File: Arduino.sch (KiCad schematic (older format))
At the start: 0 parts

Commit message: Overall Schematic
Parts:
- added R? (x13): R, ~, symbol R
- added U?: ARDUINOPINS, symbol ARDUINOPINS
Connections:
- net MISO: now also R?.2
- net MOSI: now also R?.2
- net SCLK: now also R?.2
- net TACH_MEAS: now also R?.1
- new net: R?.1, U?.11 (Digital0)
- new net: R?.1, U?.12 (Digital1)
- new net: R?.1, U?.19 (Digital8)
- new net: R?.1, U?.20 (PWM0)
- new net: R?.1, U?.21 (CS_N)
- new net: R?.1, U?.22 (MOSI)
- new net: R?.1, U?.23 (MISO)
- new net: R?.1, U?.24 (SCK)
- new net: R?.2, U?.5 (AnalogIn0)
- new net: R?.2, U?.6 (AnalogIn1)
- new net: R?.2, U?.7 (AnalogIn2)
- new net: R?.2, U?.8 (AnalogIn3)
- new net ADC_CS_N: R?.2
- new net CURR_MEAS: R?.1
- new net DAC_CS_N: R?.2
- new net FAN_EN_N: R?.2
- new net GND: R?.1
- new net LED_EN_PWM: R?.2
- new net RELAY+: R?.2
- new net RELAY-: R?.2
- new net V+_ADJ_MON: R?.1
- new net V-_ADJ_MON: R?.1
- no-connect marks 0 -> 1

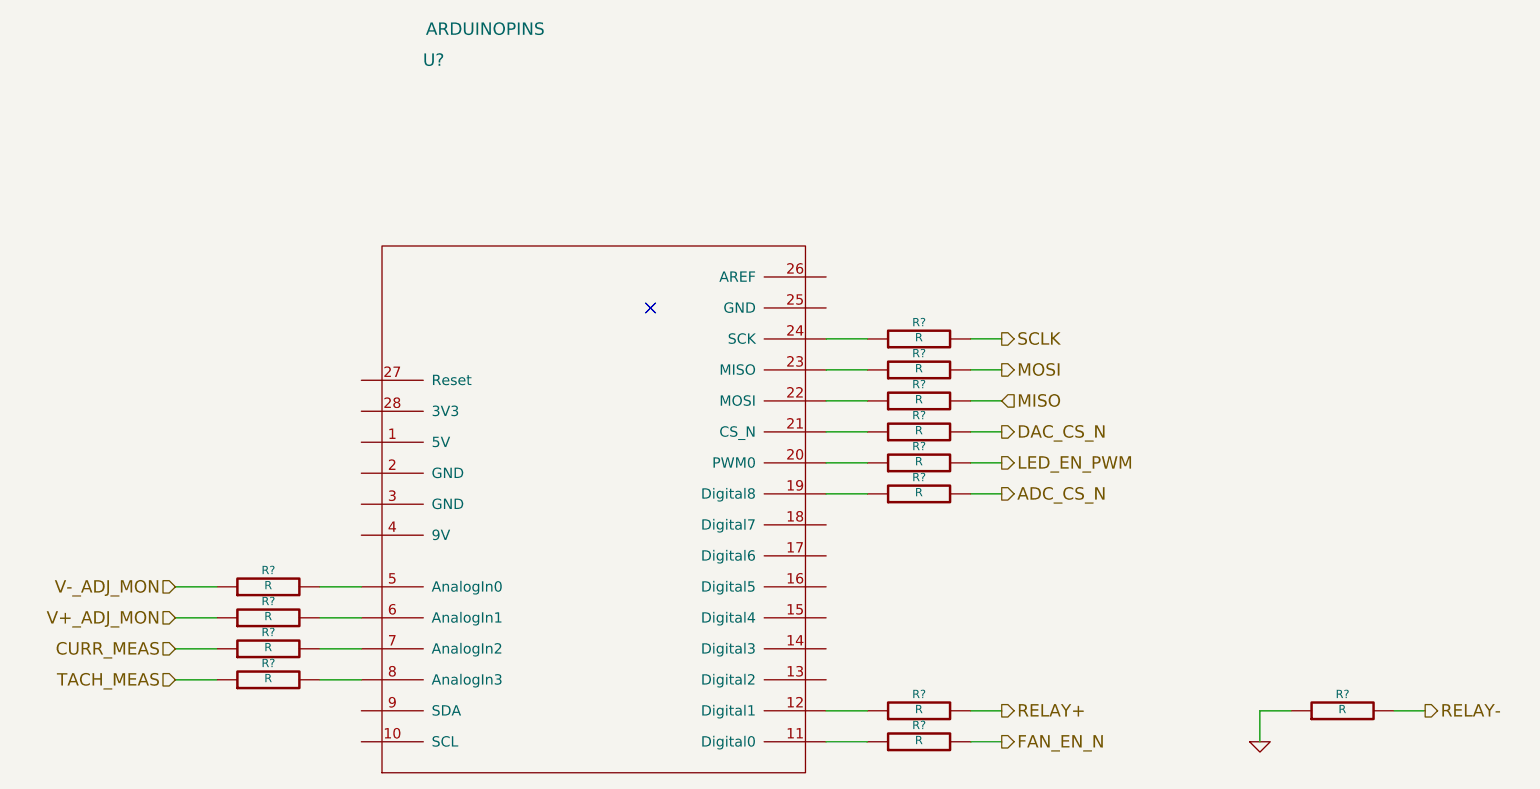
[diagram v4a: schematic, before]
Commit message: Fan/Current Module Refactoring
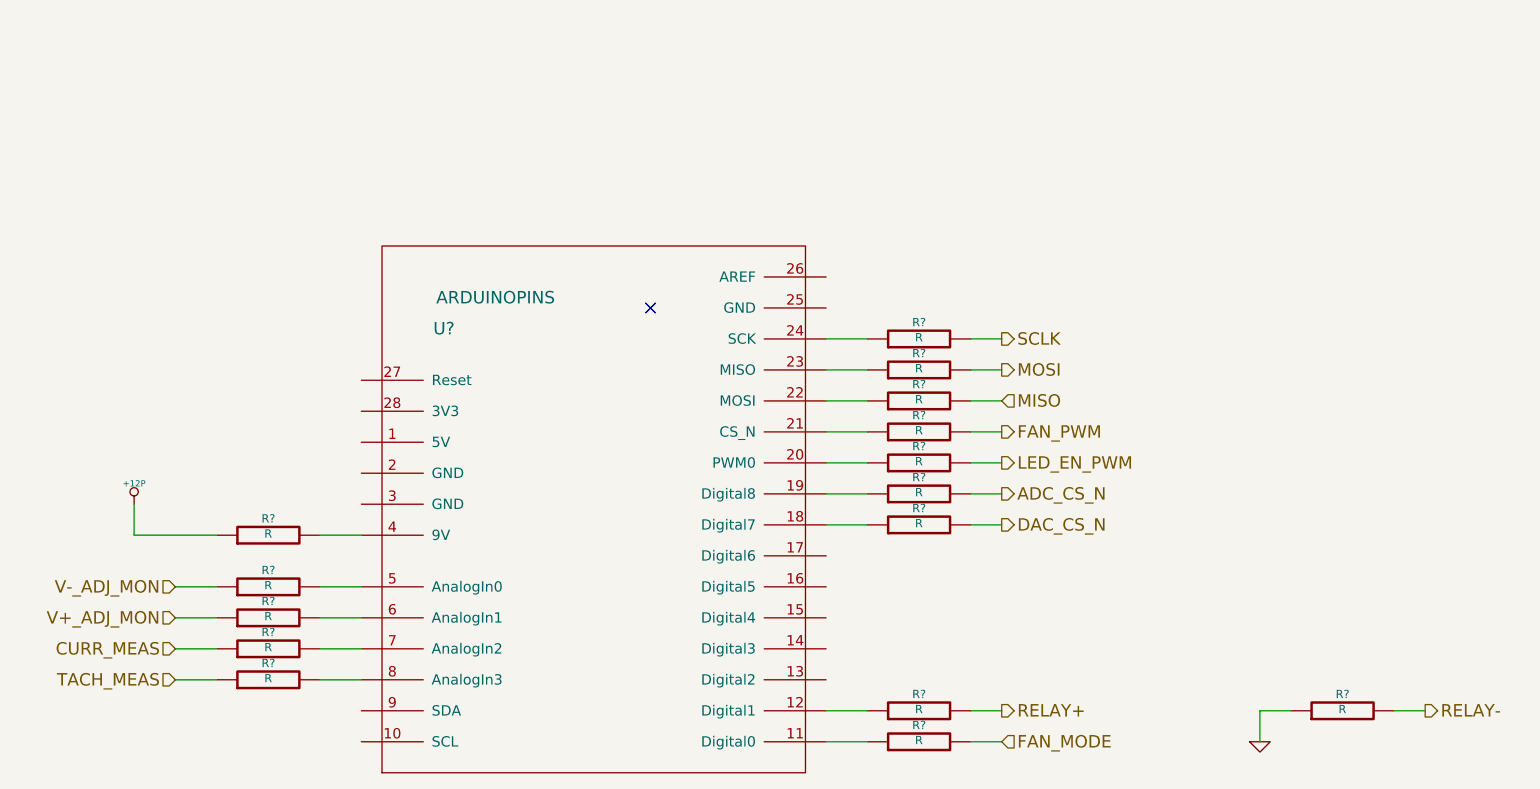
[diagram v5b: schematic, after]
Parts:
- added R? (x2): R, ~, symbol R
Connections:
- net at U?.11 (Digital0): now also R?.1; no longer R?.1
- net at U?.18 (Digital7): now also R?.1
- net at U?.21 (CS_N): now also R?.1; no longer R?.1
- net at U?.4 (9V): now also R?.2
- net FAN_EN_N renamed FAN_PWM
- new net +12P: R?.1
- new net FAN_MODE: R?.2
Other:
- moved on the sheet: R?
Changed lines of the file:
@@
 $Descr A4 11693 8268
 encoding utf-8
-Sheet 2 9
+Sheet 8 9
 Title ""
-Date "28 sep 2013"
+Date "30 sep 2013"
 Rev ""
 Comp ""
@@
 Comment4 ""
 $EndDescr
-Text HLabel 7300 5900 2    60   Output ~ 0
-FAN_EN_N
+Text HLabel 7300 4400 2    60   Output ~ 0
+FAN_PWM
 Text HLabel 3300 5600 0    60   Input ~ 0
 TACH_MEAS
@@
 Text HLabel 7300 3950 2    60   Output ~ 0
 SCLK
-Text HLabel 7300 4400 2    60   Output ~ 0
+Text HLabel 7300 4850 2    60   Output ~ 0
 DAC_CS_N
 Text HLabel 7300 5750 2    60   Output ~ 0
@@
 U 1 1 524756E9
 P 5350 4800
-F 0 "U?" H 4550 7000 60  0000 C CNN
-F 1 "ARDUINOPINS" H 4800 7150 60  0000 C CNN
+F 0 "U?" H 4600 5700 60  0000 C CNN
+F 1 "ARDUINOPINS" H 4850 5850 60  0000 C CNN
 F 2 "" H 5350 4800 60  0000 C CNN
 F 3 "" H 5350 4800 60  0000 C CNN
@@
 L R R?
 U 1 1 5247573B
-P 6900 5900
-F 0 "R?" V 6980 5900 40  0000 C CNN
-F 1 "R" V 6907 5901 40  0000 C CNN
-F 2 "~" V 6830 5900 30  0000 C CNN
-F 3 "~" H 6900 5900 30  0000 C CNN
-	1    6900 5900
-	0    -1   -1   0
-$EndComp
-Wire Wire Line
-	7150 5900 7300 5900
-Wire Wire Line
-	6650 5900 6450 5900
+P 6900 4400
+F 0 "R?" V 6980 4400 40  0000 C CNN
+F 1 "R" V 6907 4401 40  0000 C CNN
+F 2 "~" V 6830 4400 30  0000 C CNN
+F 3 "~" H 6900 4400 30  0000 C CNN
+	1    6900 4400
+	0    -1   -1   0
+$EndComp
+Wire Wire Line
+	7150 4400 7300 4400
+Wire Wire Line
+	6650 4400 6450 4400
 $Comp
 L R R?
@@
 L R R?
 U 1 1 5247E718
-P 6900 4400
-F 0 "R?" V 6980 4400 40  0000 C CNN
-F 1 "R" V 6907 4401 40  0000 C CNN
-F 2 "~" V 6830 4400 30  0000 C CNN
-F 3 "~" H 6900 4400 30  0000 C CNN
-	1    6900 4400
+P 6900 4850
+F 0 "R?" V 6980 4850 40  0000 C CNN
+F 1 "R" V 6907 4851 40  0000 C CNN
+F 2 "~" V 6830 4850 30  0000 C CNN
+F 3 "~" H 6900 4850 30  0000 C CNN
+	1    6900 4850
 	0    -1   -1   0
 $EndComp
@@
 	7150 4250 7300 4250
 Wire Wire Line
-	7150 4400 7300 4400
-Wire Wire Line
 	6450 3950 6650 3950
 Wire Wire Line
@@
 Wire Wire Line
 	6450 4250 6650 4250
-Wire Wire Line
-	6450 4400 6650 4400
 $Comp
 L R R?
@@
 Wire Wire Line
 	6650 4700 6450 4700
+Wire Wire Line
+	7150 4850 7300 4850
+Wire Wire Line
+	6450 4850 6650 4850
+Text HLabel 7300 5900 2    60   Input ~ 0
+FAN_MODE
+$Comp
+L R R?
+U 1 1 524B6E8B
+P 6900 5900
+F 0 "R?" V 6980 5900 40  0000 C CNN
+F 1 "R" V 6907 5901 40  0000 C CNN
+F 2 "~" V 6830 5900 30  0000 C CNN
+F 3 "~" H 6900 5900 30  0000 C CNN
+	1    6900 5900
+	0    -1   -1   0
+$EndComp
+Wire Wire Line
+	6450 5900 6650 5900
+Wire Wire Line
+	7150 5900 7300 5900
+$Comp
+L R R?
+U 1 1 524B7119
+P 3750 4900
+F 0 "R?" V 3830 4900 40  0000 C CNN
+F 1 "R" V 3757 4901 40  0000 C CNN
+F 2 "~" V 3680 4900 30  0000 C CNN
+F 3 "~" H 3750 4900 30  0000 C CNN
+	1    3750 4900
+	0    -1   -1   0
+$EndComp
+Wire Wire Line
+	3500 4900 3100 4900
+Wire Wire Line
+	3100 4900 3100 4750
+Wire Wire Line
+	4000 4900 4200 4900
+$Comp
+L +12P #PWR?
+U 1 1 524B7161
+P 3100 4750
+F 0 "#PWR?" H 3100 4720 30  0001 C CNN
+F 1 "+12P" H 3100 4850 30  0000 C CNN
+F 2 "" H 3100 4750 60  0000 C CNN
+F 3 "" H 3100 4750 60  0000 C CNN
+	1    3100 4750
+	1    0    0    -1
+$EndComp
 $EndSCHEMATC

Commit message: Preliminary Module Layouts
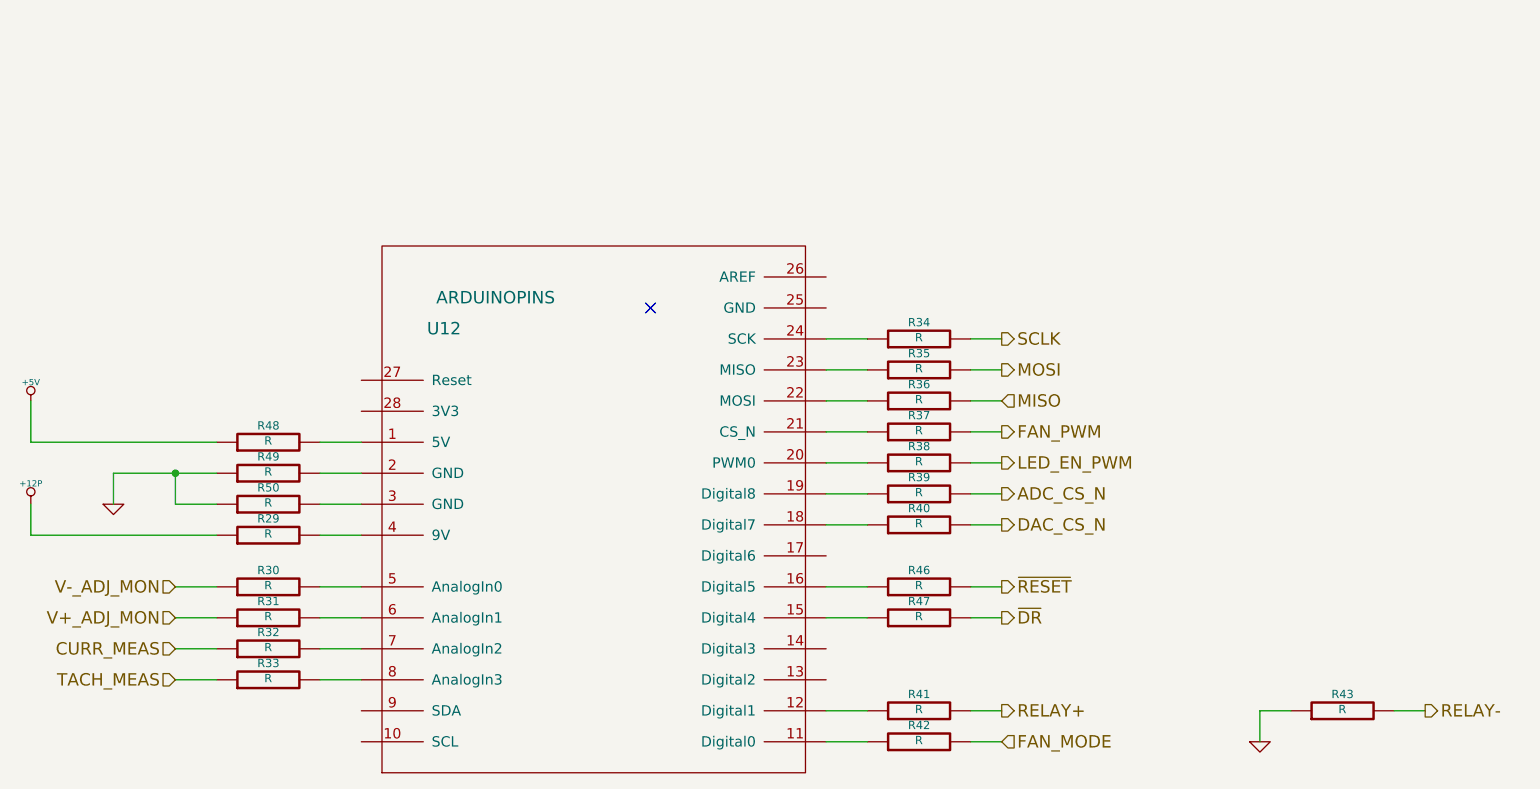
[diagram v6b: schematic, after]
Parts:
- added R46, R47, R48, R49, R50: R, ~, symbol R
- gave numbers to parts that had none: 16
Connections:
- net GND: now also R49.1, R50.1
- net at U12.1 (5V): now also R48.2
- net at U12.15 (Digital4): now also R47.1
- net at U12.16 (Digital5): now also R46.1
- net at U12.2 (GND): now also R49.2
- net at U12.3 (GND): now also R50.2
- new net +5V: R48.1
- new net ~DR: R47.2
- new net ~RESET: R46.2
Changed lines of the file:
@@
 Sheet 8 9
 Title ""
-Date "30 sep 2013"
+Date "15 oct 2013"
 Rev ""
 Comp ""
@@
 NoConn ~ 5600 3800
 $Comp
-L ARDUINOPINS U?
+L ARDUINOPINS U12
 U 1 1 524756E9
 P 5350 4800
-F 0 "U?" H 4600 5700 60  0000 C CNN
+F 0 "U12" H 4600 5700 60  0000 C CNN
 F 1 "ARDUINOPINS" H 4850 5850 60  0000 C CNN
 F 2 "" H 5350 4800 60  0000 C CNN
@@
 CURR_MEAS
 $Comp
-L R R?
+L R R37
 U 1 1 5247573B
 P 6900 4400
-F 0 "R?" V 6980 4400 40  0000 C CNN
+F 0 "R37" V 6980 4400 40  0000 C CNN
 F 1 "R" V 6907 4401 40  0000 C CNN
 F 2 "~" V 6830 4400 30  0000 C CNN
@@
 	6650 4400 6450 4400
 $Comp
-L R R?
+L R R41
 U 1 1 5247DC4C
 P 6900 5750
-F 0 "R?" V 6980 5750 40  0000 C CNN
+F 0 "R41" V 6980 5750 40  0000 C CNN
 F 1 "R" V 6907 5751 40  0000 C CNN
 F 2 "~" V 6830 5750 30  0000 C CNN
@@
 	8550 5750 8550 5900
 $Comp
-L GND #PWR?
+L GND #PWR053
 U 1 1 5247DC74
 P 8550 5900
-F 0 "#PWR?" H 8550 5900 30  0001 C CNN
+F 0 "#PWR053" H 8550 5900 30  0001 C CNN
 F 1 "GND" H 8550 5830 30  0001 C CNN
 F 2 "" H 8550 5900 60  0000 C CNN
@@
 $EndComp
 $Comp
-L R R?
+L R R32
 U 1 1 5247DC8B
 P 3750 5450
-F 0 "R?" V 3830 5450 40  0000 C CNN
+F 0 "R32" V 3830 5450 40  0000 C CNN
 F 1 "R" V 3757 5451 40  0000 C CNN
 F 2 "~" V 3680 5450 30  0000 C CNN
@@
 $EndComp
 $Comp
-L R R?
+L R R33
 U 1 1 5247DC91
 P 3750 5600
-F 0 "R?" V 3830 5600 40  0000 C CNN
+F 0 "R33" V 3830 5600 40  0000 C CNN
 F 1 "R" V 3757 5601 40  0000 C CNN
 F 2 "~" V 3680 5600 30  0000 C CNN
@@
 V-_ADJ_MON
 $Comp
-L R R?
+L R R30
 U 1 1 5247E210
 P 3750 5150
-F 0 "R?" V 3830 5150 40  0000 C CNN
+F 0 "R30" V 3830 5150 40  0000 C CNN
 F 1 "R" V 3757 5151 40  0000 C CNN
 F 2 "~" V 3680 5150 30  0000 C CNN
@@
 $EndComp
 $Comp
-L R R?
+L R R31
 U 1 1 5247E216
 P 3750 5300
-F 0 "R?" V 3830 5300 40  0000 C CNN
+F 0 "R31" V 3830 5300 40  0000 C CNN
 F 1 "R" V 3757 5301 40  0000 C CNN
 F 2 "~" V 3680 5300 30  0000 C CNN
@@
 	4000 5300 4200 5300
 $Comp
-L R R?
+L R R34
 U 1 1 5247E706
 P 6900 3950
-F 0 "R?" V 6980 3950 40  0000 C CNN
+F 0 "R34" V 6980 3950 40  0000 C CNN
 F 1 "R" V 6907 3951 40  0000 C CNN
 F 2 "~" V 6830 3950 30  0000 C CNN
@@
 $EndComp
 $Comp
-L R R?
+L R R35
 U 1 1 5247E70C
 P 6900 4100
-F 0 "R?" V 6980 4100 40  0000 C CNN
+F 0 "R35" V 6980 4100 40  0000 C CNN
 F 1 "R" V 6907 4101 40  0000 C CNN
 F 2 "~" V 6830 4100 30  0000 C CNN
@@
 $EndComp
 $Comp
-L R R?
+L R R36
 U 1 1 5247E712
 P 6900 4250
-F 0 "R?" V 6980 4250 40  0000 C CNN
+F 0 "R36" V 6980 4250 40  0000 C CNN
 F 1 "R" V 6907 4251 40  0000 C CNN
 F 2 "~" V 6830 4250 30  0000 C CNN
@@
 $EndComp
 $Comp
-L R R?
+L R R40
 U 1 1 5247E718
 P 6900 4850
-F 0 "R?" V 6980 4850 40  0000 C CNN
+F 0 "R40" V 6980 4850 40  0000 C CNN
 F 1 "R" V 6907 4851 40  0000 C CNN
 F 2 "~" V 6830 4850 30  0000 C CNN
@@
 	6450 4250 6650 4250
 $Comp
-L R R?
+L R R43
 U 1 1 5247EA04
 P 8950 5750
-F 0 "R?" V 9030 5750 40  0000 C CNN
+F 0 "R43" V 9030 5750 40  0000 C CNN
 F 1 "R" V 8957 5751 40  0000 C CNN
 F 2 "~" V 8880 5750 30  0000 C CNN
@@
 LED_EN_PWM
 $Comp
-L R R?
+L R R38
 U 1 1 5247EC74
 P 6900 4550
-F 0 "R?" V 6980 4550 40  0000 C CNN
+F 0 "R38" V 6980 4550 40  0000 C CNN
 F 1 "R" V 6907 4551 40  0000 C CNN
 F 2 "~" V 6830 4550 30  0000 C CNN
@@
 	6450 4550 6650 4550
 $Comp
-L R R?
+L R R39
 U 1 1 5249FE11
 P 6900 4700
-F 0 "R?" V 6980 4700 40  0000 C CNN
+F 0 "R39" V 6980 4700 40  0000 C CNN
 F 1 "R" V 6907 4701 40  0000 C CNN
 F 2 "~" V 6830 4700 30  0000 C CNN
@@
 FAN_MODE
 $Comp
-L R R?
+L R R42
 U 1 1 524B6E8B
 P 6900 5900
-F 0 "R?" V 6980 5900 40  0000 C CNN
+F 0 "R42" V 6980 5900 40  0000 C CNN
 F 1 "R" V 6907 5901 40  0000 C CNN
 F 2 "~" V 6830 5900 30  0000 C CNN
@@
 	7150 5900 7300 5900
 $Comp
-L R R?
+L R R29
 U 1 1 524B7119
 P 3750 4900
-F 0 "R?" V 3830 4900 40  0000 C CNN
+F 0 "R29" V 3830 4900 40  0000 C CNN
 F 1 "R" V 3757 4901 40  0000 C CNN
 F 2 "~" V 3680 4900 30  0000 C CNN
@@
 $EndComp
 Wire Wire Line
-	3500 4900 3100 4900
-Wire Wire Line
-	3100 4900 3100 4750
+	3500 4900 2600 4900
+Wire Wire Line
+	2600 4900 2600 4750
 Wire Wire Line
 	4000 4900 4200 4900
 $Comp
-L +12P #PWR?
+L +12P #PWR054
 U 1 1 524B7161
-P 3100 4750
-F 0 "#PWR?" H 3100 4720 30  0001 C CNN
-F 1 "+12P" H 3100 4850 30  0000 C CNN
-F 2 "" H 3100 4750 60  0000 C CNN
-F 3 "" H 3100 4750 60  0000 C CNN
-	1    3100 4750
+P 2600 4750
+F 0 "#PWR054" H 2600 4720 30  0001 C CNN
+F 1 "+12P" H 2600 4850 30  0000 C CNN
+F 2 "" H 2600 4750 60  0000 C CNN
+F 3 "" H 2600 4750 60  0000 C CNN
+	1    2600 4750
 	1    0    0    -1
 $EndComp
+$Comp
+L R R46
+U 1 1 525BB685
+P 6900 5150
+F 0 "R46" V 6980 5150 40  0000 C CNN
+F 1 "R" V 6907 5151 40  0000 C CNN
+F 2 "~" V 6830 5150 30  0000 C CNN
+F 3 "~" H 6900 5150 30  0000 C CNN
+	1    6900 5150
+	0    -1   -1   0
+$EndComp
+$Comp
+L R R47
+U 1 1 525BB68B
+P 6900 5300
+F 0 "R47" V 6980 5300 40  0000 C CNN
+F 1 "R" V 6907 5301 40  0000 C CNN
+F 2 "~" V 6830 5300 30  0000 C CNN
+F 3 "~" H 6900 5300 30  0000 C CNN
+	1    6900 5300
+	0    -1   -1   0
+$EndComp
+Wire Wire Line
+	6450 5150 6650 5150
+Wire Wire Line
+	6650 5300 6450 5300
+Wire Wire Line
+	7150 5150 7300 5150
+Wire Wire Line
+	7150 5300 7300 5300
+Text HLabel 7300 5150 2    60   Output ~ 0
+~RESET
+Text HLabel 7300 5300 2    60   Output ~ 0
+~DR
+$Comp
+L R R50
+U 1 1 525DA883
+P 3750 4750
+F 0 "R50" V 3830 4750 40  0000 C CNN
+F 1 "R" V 3757 4751 40  0000 C CNN
+F 2 "~" V 3680 4750 30  0000 C CNN
+F 3 "~" H 3750 4750 30  0000 C CNN
+	1    3750 4750
+	0    -1   -1   0
+$EndComp
+$Comp
+L R R49
+U 1 1 525DA889
+P 3750 4600
+F 0 "R49" V 3830 4600 40  0000 C CNN
+F 1 "R" V 3757 4601 40  0000 C CNN
+F 2 "~" V 3680 4600 30  0000 C CNN
+F 3 "~" H 3750 4600 30  0000 C CNN
+	1    3750 4600
+	0    -1   -1   0
+$EndComp
+$Comp
+L R R48
+U 1 1 525DA88F
+P 3750 4450
+F 0 "R48" V 3830 4450 40  0000 C CNN
+F 1 "R" V 3757 4451 40  0000 C CNN
+F 2 "~" V 3680 4450 30  0000 C CNN
+F 3 "~" H 3750 4450 30  0000 C CNN
+	1    3750 4450
+	0    -1   -1   0
+$EndComp
+Wire Wire Line
+	2600 4450 3500 4450
+Wire Wire Line
+	2600 4250 2600 4450
+Wire Wire Line
+	3500 4750 3300 4750
+Wire Wire Line
+	3300 4750 3300 4600
+Wire Wire Line
+	3000 4600 3500 4600
+Wire Wire Line
+	3000 4600 3000 4750
+Connection ~ 3300 4600
+$Comp
+L GND #PWR055
+U 1 1 525DA913
+P 3000 4750
+F 0 "#PWR055" H 3000 4750 30  0001 C CNN
+F 1 "GND" H 3000 4680 30  0001 C CNN
+F 2 "" H 3000 4750 60  0000 C CNN
+F 3 "" H 3000 4750 60  0000 C CNN
+	1    3000 4750
+	1    0    0    -1
+$EndComp
+$Comp
+L +5V #PWR056
+U 1 1 525DA94E
+P 2600 4250
+F 0 "#PWR056" H 2600 4340 20  0001 C CNN
+F 1 "+5V" H 2600 4340 30  0000 C CNN
+F 2 "" H 2600 4250 60  0000 C CNN
+F 3 "" H 2600 4250 60  0000 C CNN
+	1    2600 4250
+	1    0    0    -1
+$EndComp
+Wire Wire Line
+	4000 4450 4200 4450
+Wire Wire Line
+	4200 4600 4000 4600
+Wire Wire Line
+	4000 4750 4200 4750
 $EndSCHEMATC

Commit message: Power Modification Module
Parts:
- added R24, R51: R, ~, symbol R
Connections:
- net at U12.13 (Digital2): now also R51.1
- net at U12.14 (Digital3): now also R24.1
- net ADC_CS_N renamed ~ADC_CS
- net DAC_CS_N renamed ~DAC_CS
- new net ~LDAC: R24.2
- new net ~SHDN: R51.2
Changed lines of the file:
@@
 Sheet 8 9
 Title ""
-Date "17 oct 2013"
+Date "27 oct 2013"
 Rev ""
 Comp ""
@@
 SCLK
 Text HLabel 7300 4850 2    60   Output ~ 0
-DAC_CS_N
+~DAC_CS
 Text HLabel 7300 5750 2    60   Output ~ 0
 RELAY+
@@
 	8550 5750 8550 5900
 $Comp
-L GND #PWR053
+L GND #PWR66
 U 1 1 5247DC74
 P 8550 5900
-F 0 "#PWR053" H 8550 5900 30  0001 C CNN
+F 0 "#PWR66" H 8550 5900 30  0001 C CNN
 F 1 "GND" H 8550 5830 30  0001 C CNN
 F 2 "" H 8550 5900 60  0000 C CNN
@@
 $EndComp
 Text HLabel 7300 4700 2    60   Output ~ 0
-ADC_CS_N
+~ADC_CS
 Wire Wire Line
 	7300 4700 7150 4700
@@
 	4000 4900 4200 4900
 $Comp
-L +12P #PWR054
+L +12P #PWR64
 U 1 1 524B7161
 P 2600 4750
-F 0 "#PWR054" H 2600 4720 30  0001 C CNN
+F 0 "#PWR64" H 2600 4720 30  0001 C CNN
 F 1 "+12P" H 2600 4850 30  0000 C CNN
 F 2 "" H 2600 4750 60  0000 C CNN
@@
 Connection ~ 3300 4600
 $Comp
-L GND #PWR055
+L GND #PWR65
 U 1 1 525DA913
 P 3000 4750
-F 0 "#PWR055" H 3000 4750 30  0001 C CNN
+F 0 "#PWR65" H 3000 4750 30  0001 C CNN
 F 1 "GND" H 3000 4680 30  0001 C CNN
 F 2 "" H 3000 4750 60  0000 C CNN
@@
 $EndComp
 $Comp
-L +5V #PWR056
+L +5V #PWR63
 U 1 1 525DA94E
 P 2600 4250
-F 0 "#PWR056" H 2600 4340 20  0001 C CNN
+F 0 "#PWR63" H 2600 4340 20  0001 C CNN
 F 1 "+5V" H 2600 4340 30  0000 C CNN
 F 2 "" H 2600 4250 60  0000 C CNN
@@
 Wire Wire Line
 	4000 4750 4200 4750
+$Comp
+L R R24
+U 1 1 526430CB
+P 6900 5450
+F 0 "R24" V 6980 5450 40  0000 C CNN
+F 1 "R" V 6907 5451 40  0000 C CNN
+F 2 "~" V 6830 5450 30  0000 C CNN
+F 3 "~" H 6900 5450 30  0000 C CNN
+	1    6900 5450
+	0    -1   -1   0
+$EndComp
+$Comp
+L R R51
+U 1 1 526430D1
+P 6900 5600
+F 0 "R51" V 6980 5600 40  0000 C CNN
+F 1 "R" V 6907 5601 40  0000 C CNN
+F 2 "~" V 6830 5600 30  0000 C CNN
+F 3 "~" H 6900 5600 30  0000 C CNN
+	1    6900 5600
+	0    -1   -1   0
+$EndComp
+Wire Wire Line
+	6450 5450 6650 5450
+Wire Wire Line
+	6450 5600 6650 5600
+Text HLabel 7300 5450 2    60   Output ~ 0
+~LDAC
+Text HLabel 7300 5600 2    60   Output ~ 0
+~SHDN
+Wire Wire Line
+	7150 5450 7300 5450
+Wire Wire Line
+	7150 5600 7300 5600
 $EndSCHEMATC
